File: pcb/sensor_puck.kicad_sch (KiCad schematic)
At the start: 35 parts, among them J1 Conn_01x07_Socket, J2 Conn_01x07_Socket, J3 USB_C_Receptacle_USB2.0_16P, SW1 RST, SW2 BOOT, U1 ESP32-S3-MINI-1U, U2 LIS3MDL, U3 LSM6DSOXTR, U4 STC31-C-R3

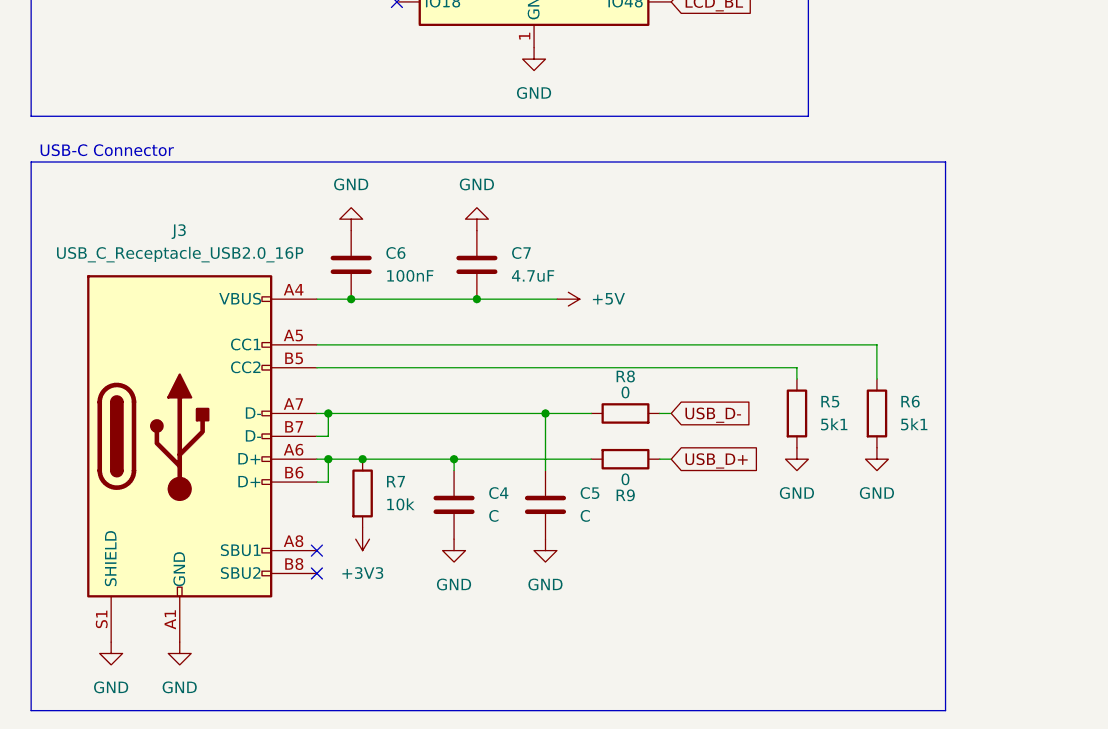
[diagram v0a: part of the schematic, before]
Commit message: fix(pcb): improve USB-C wiring and routing
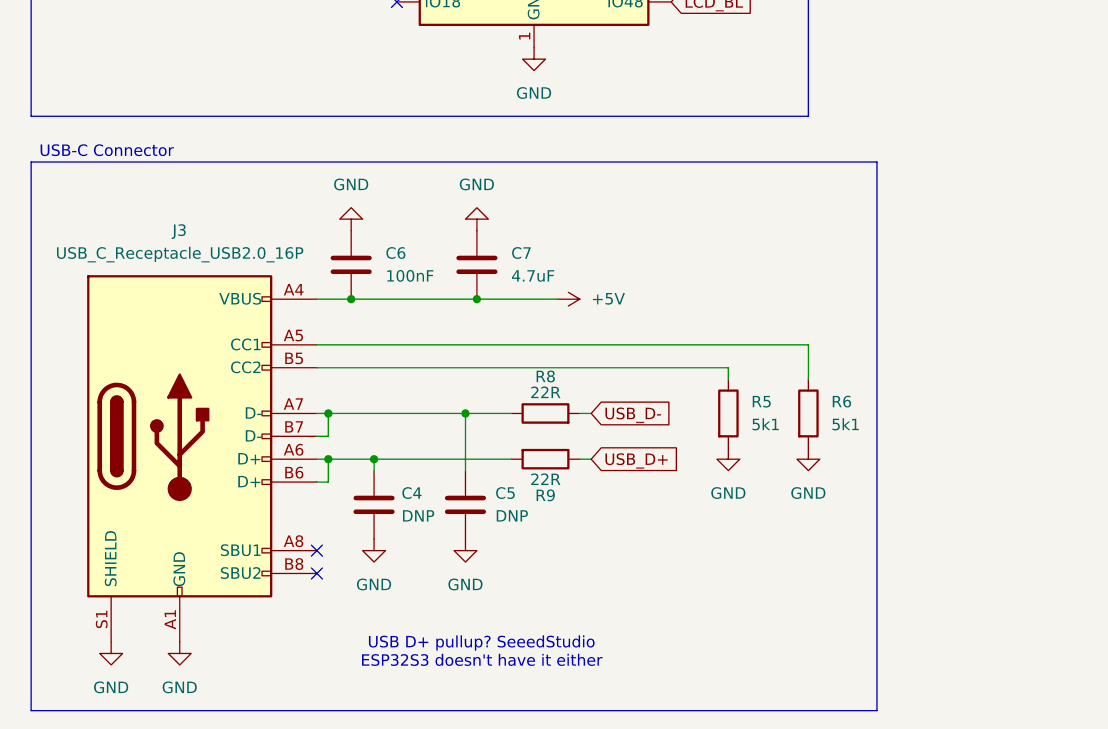
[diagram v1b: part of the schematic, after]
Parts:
- removed R7: 10k, Resistor_SMD:R_0805_2012Metric, symbol Device:R
- C4, C5: value C -> DNP
- R8, R9: value 0 -> 22R
- SW1, SW2: footprint Button_Switch_SMD:SW_Push_1P1T_NO_6x6mm_H9.5mm -> Button_Switch_THT:SW_PUSH_6mm
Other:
- note added: "USB D+ pullup? SeeedStudio ESP32S3 doesn't have it either"
- moved on the sheet: C4, C5, R5, R6, R8, R9

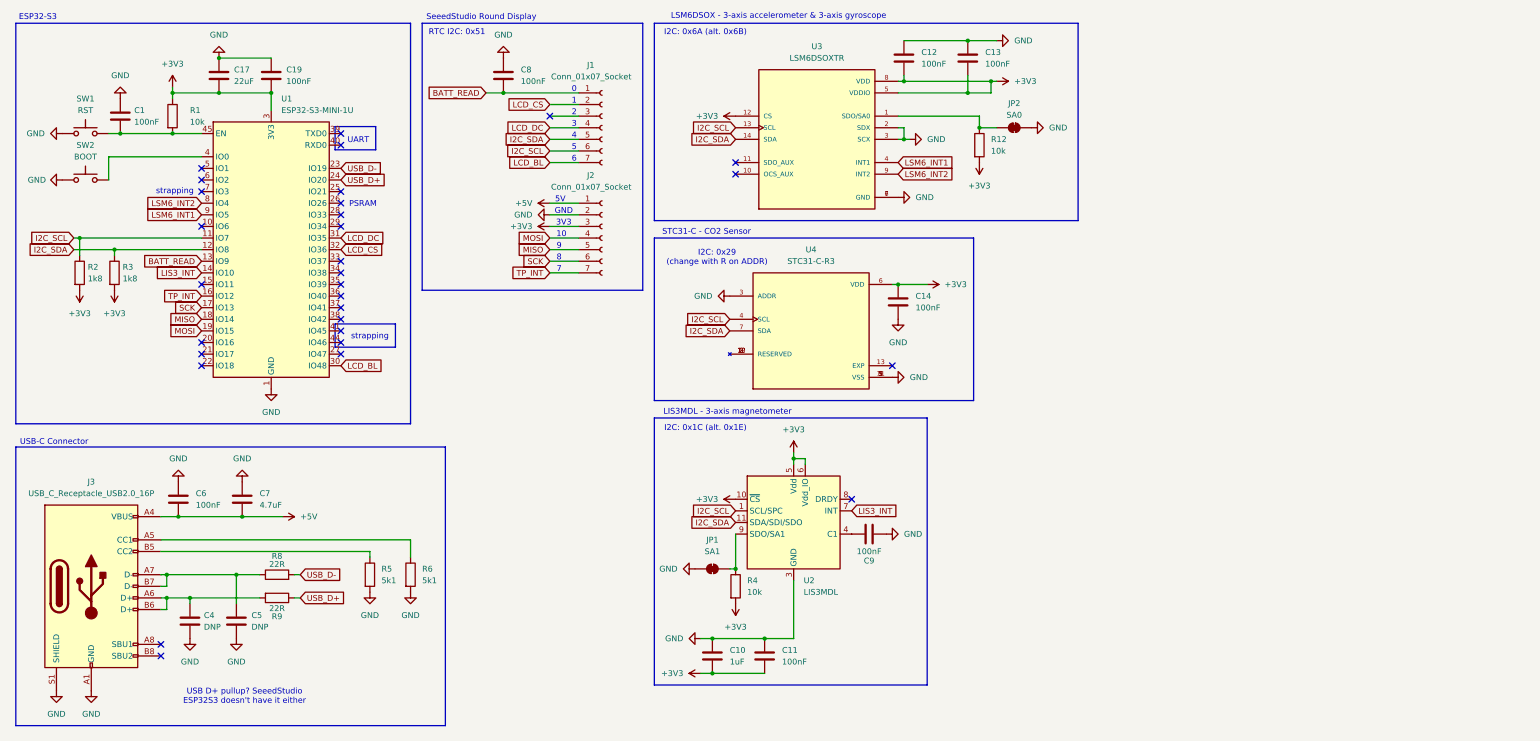
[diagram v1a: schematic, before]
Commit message: feat(pcb): VBUS -> 3V3 regulator, BME288, general improvements
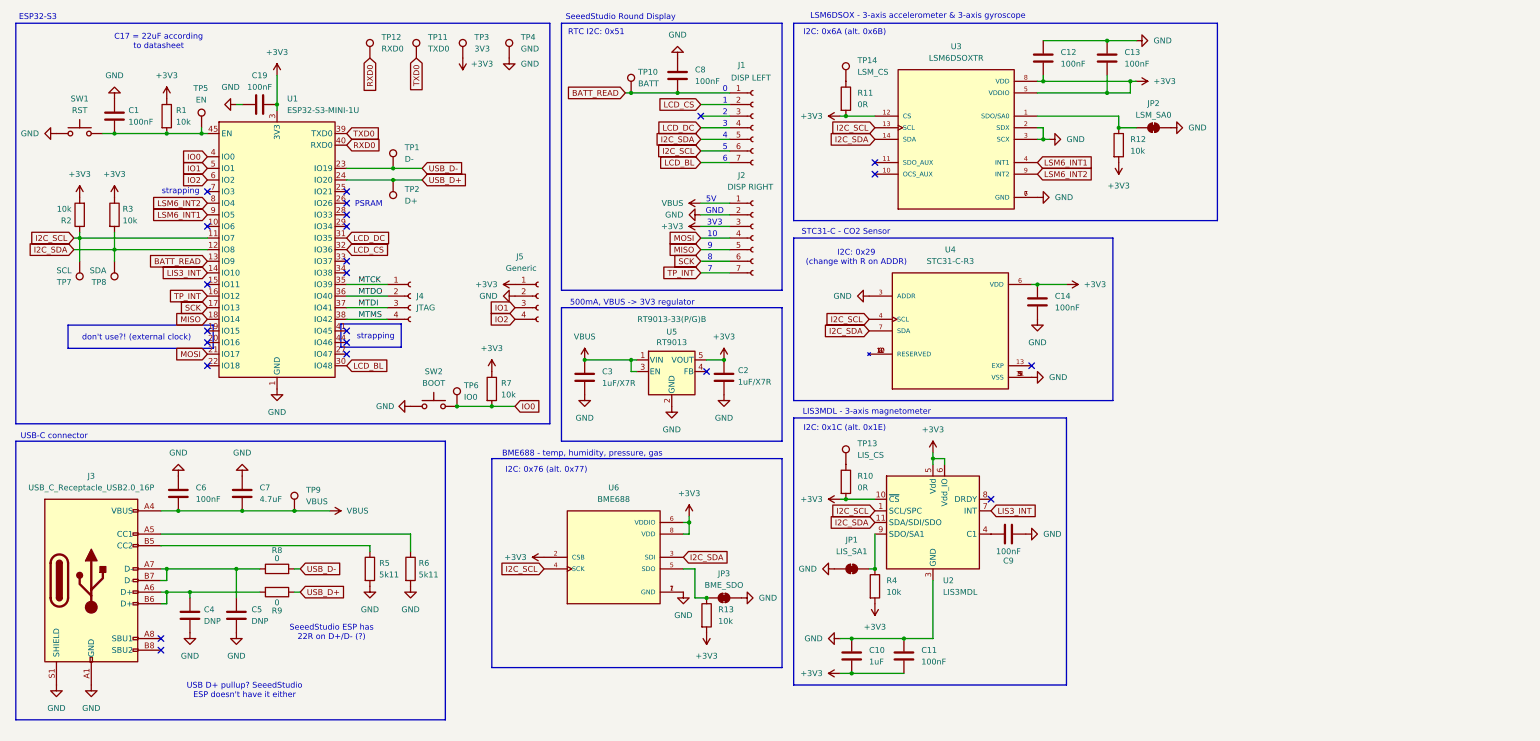
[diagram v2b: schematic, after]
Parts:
- removed C17: 22uF, Capacitor_SMD:C_0805_2012Metric, symbol Device:C
- added C2, C3: 1uF/X7R, Capacitor_SMD:C_0805_2012Metric, symbol Device:C
- added J4: JTAG, Connector_PinHeader_2.54mm:PinHeader_1x04_P2.54mm_Vertical, symbol Connector:Conn_01x04_Socket
- added J5: Generic, Connector_PinHeader_2.54mm:PinHeader_1x04_P2.54mm_Vertical, symbol Connector:Conn_01x04_Socket
- added JP3: BME_SDO, Jumper:SolderJumper-2_P1.3mm_Bridged_RoundedPad1.0x1.5mm, symbol Jumper:SolderJumper_2_Bridged
- added R10, R11: 0R, Resistor_SMD:R_0805_2012Metric, symbol Device:R
- added R13, R7: 10k, Resistor_SMD:R_0805_2012Metric, symbol Device:R
- added TP1: D-, TestPoint:TestPoint_Pad_D1.0mm, symbol Connector:TestPoint
- added TP10: BATT, TestPoint:TestPoint_Pad_D1.0mm, symbol Connector:TestPoint
- added TP11: TXD0, TestPoint:TestPoint_Pad_D1.0mm, symbol Connector:TestPoint
- added TP12: RXD0, TestPoint:TestPoint_Pad_D1.0mm, symbol Connector:TestPoint
- added TP13: LIS_CS, TestPoint:TestPoint_Pad_1.0x1.0mm, symbol Connector:TestPoint
- added TP14: LSM_CS, TestPoint:TestPoint_Pad_1.0x1.0mm, symbol Connector:TestPoint
- added TP2: D+, TestPoint:TestPoint_Pad_D1.0mm, symbol Connector:TestPoint
- added TP3: 3V3, TestPoint:TestPoint_Pad_D1.0mm, symbol Connector:TestPoint
- added TP4: GND, TestPoint:TestPoint_Pad_D1.0mm, symbol Connector:TestPoint
- added TP5: EN, TestPoint:TestPoint_Pad_D1.0mm, symbol Connector:TestPoint
- added TP6: IO0, TestPoint:TestPoint_Pad_D1.0mm, symbol Connector:TestPoint
- added TP7: SCL, TestPoint:TestPoint_Pad_D1.0mm, symbol Connector:TestPoint
- added TP8: SDA, TestPoint:TestPoint_Pad_D1.0mm, symbol Connector:TestPoint
- added TP9: VBUS, TestPoint:TestPoint_Pad_D1.0mm, symbol Connector:TestPoint
- added U5: RT9013, Package_TO_SOT_SMD:SOT-23-5, symbol Regulator_Linear:TPS72201
- added U6: BME688, BME688:IC_BME688, symbol BME688:BME688
- J1: value Conn_01x07_Socket -> DISP LEFT
- J2: value Conn_01x07_Socket -> DISP RIGHT
- JP1: value SA1 -> LIS_SA1; footprint Jumper:SolderJumper-2_P1.3mm_Bridged_Pad1.0x1.5mm -> Jumper:SolderJumper-2_P1.3mm_Bridged_RoundedPad1.0x1.5mm
- JP2: value SA0 -> LSM_SA0; footprint Jumper:SolderJumper-2_P1.3mm_Bridged_Pad1.0x1.5mm -> Jumper:SolderJumper-2_P1.3mm_Bridged_RoundedPad1.0x1.5mm
- R2, R3: value 1k8 -> 10k
- R5, R6: value 5k1 -> 5k11
- R8, R9: value 22R -> 0
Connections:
- net +3V3: now also R3.1, C2.2, J5.1 (Pin_1), R10.2, R11.2, R13.2, R7.1, TP3.1, U5.5 (VOUT), U6.2 (CSB), U6.6 (VDDIO), U6.8 (VDD); no longer R3.2
- net BATT_READ: now also TP10.1
- net GND: now also C2.1, C3.1, J5.2 (Pin_2), JP3.2 (B), TP4.1, U5.2 (GND), U6.1 (GND), U6.7 (GND)
- net I2C_SCL: now also TP7.1, U6.4 (SCK)
- net I2C_SDA: now also R3.2, TP8.1, U6.3 (SDI); no longer R3.1
- net MOSI: now also U1.21 (IO17); no longer U1.19 (IO15)
- net USB_D+: now also TP2.1
- net USB_D-: now also TP1.1
- net at C1.2, R1.2, SW1.2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: now also TP5.1
- net MTCK: now reaches U1.35 (IO39)
- net MTCK: now also J4.1 (Pin_1)
- net MTDO: now reaches U1.36 (IO40)
- net MTDO: now also J4.2 (Pin_2)
- net MTDI: now reaches U1.37 (IO41)
- net MTDI: now also J4.3 (Pin_3)
- net MTMS: now reaches U1.38 (IO42)
- net MTMS: now also J4.4 (Pin_4)
- net TXD0: now reaches U1.39 (TXD0)
- net TXD0: now also TP11.1
- net IO0: now reaches SW2.2, U1.4 (IO0)
- net IO0: now also R7.2, TP6.1
- net RXD0: now reaches U1.40 (RXD0)
- net RXD0: now also TP12.1
- net IO1: now reaches U1.5 (IO1)
- net IO1: now also J5.3 (Pin_3)
- net IO2: now reaches U1.6 (IO2)
- net IO2: now also J5.4 (Pin_4)
- net +5V renamed VBUS
- net VBUS: now also C3.2, TP9.1, U5.1 (VIN), U5.3 (EN)
- new net: JP3.1 (A), R13.1, U6.5 (SDO)
- new net: R10.1, TP13.1
- new net: R11.1, TP14.1
- no-connect marks 30 -> 23
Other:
- note added: "500mA, VBUS -> 3V3 regulator"
- note added: "BME688 - temp, humidity, pressure, gas"
- note added: "C17 = 22uF according to datasheet"
- note added: "I2C: 0x76 (alt. 0x77)"
- note added: "SeeedStudio ESP has 22R on D+/D- (?)"
- note added: "USB D+ pullup? SeeedStudio ESP doesn't have it either"
- note added: "USB-C connector"
- note added: "don't use?! (external clock)"
- note removed: "UART"
- note removed: "USB D+ pullup? SeeedStudio ESP32S3 doesn't have it either"
- note removed: "USB-C Connector"
- moved on the sheet: C1, C10, C11, C12, C13, C14, C4, C5, C6, C7, C8, C9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

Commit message: feat(pcb): route PCB
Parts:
- removed J4: JTAG, Connector_PinHeader_2.54mm:PinHeader_1x04_P2.54mm_Vertical, symbol Connector:Conn_01x04_Socket
- removed TP10: BATT, TestPoint:TestPoint_Pad_D1.0mm, symbol Connector:TestPoint
- added C15, C16: 100nF, Capacitor_SMD:C_0805_2012Metric, symbol Device:C
- added R14: 0R, Resistor_SMD:R_0805_2012Metric, symbol Device:R
- added TP15: BME_CSB, TestPoint:TestPoint_Pad_D1.0mm, symbol Connector:TestPoint
- added TP16: MTCK, TestPoint:TestPoint_Pad_D1.0mm, symbol Connector:TestPoint
- added TP17: MTDO, TestPoint:TestPoint_Pad_D1.0mm, symbol Connector:TestPoint
- added TP18: MTDI, TestPoint:TestPoint_Pad_D1.0mm, symbol Connector:TestPoint
- added TP19: MTMS, TestPoint:TestPoint_Pad_D1.0mm, symbol Connector:TestPoint
- TP13, TP14: footprint TestPoint:TestPoint_Pad_1.0x1.0mm -> TestPoint:TestPoint_Pad_D1.0mm
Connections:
- net +3V3: now also R10.1, R11.1, C15.2, C16.2, R14.2; no longer R10.2, R11.2, U2.10 (~{CS}), U3.12 (CS), U6.2 (CSB)
- net GND: now also U4.13 (EXP), C15.1, C16.1
- net at TP13.1: now also R10.2, U2.10 (~{CS}); no longer R10.1
- net at TP14.1: now also R11.2, U3.12 (CS); no longer R11.1
- net MTCK: no longer names the net of U1.35 (IO39)
- net MTCK: now also TP16.1
- net MTDI: no longer names the net of U1.37 (IO41)
- net MTDI: now also TP18.1
- net MTDO: no longer names the net of U1.36 (IO40)
- net MTDO: now also TP17.1
- net MTMS: no longer names the net of U1.38 (IO42)
- net MTMS: now also TP19.1
- new net: R14.1, TP15.1, U6.2 (CSB)
- no-connect marks 23 -> 20
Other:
- moved on the sheet: JP3, R10, R11, R13, TP13, TP14, U6

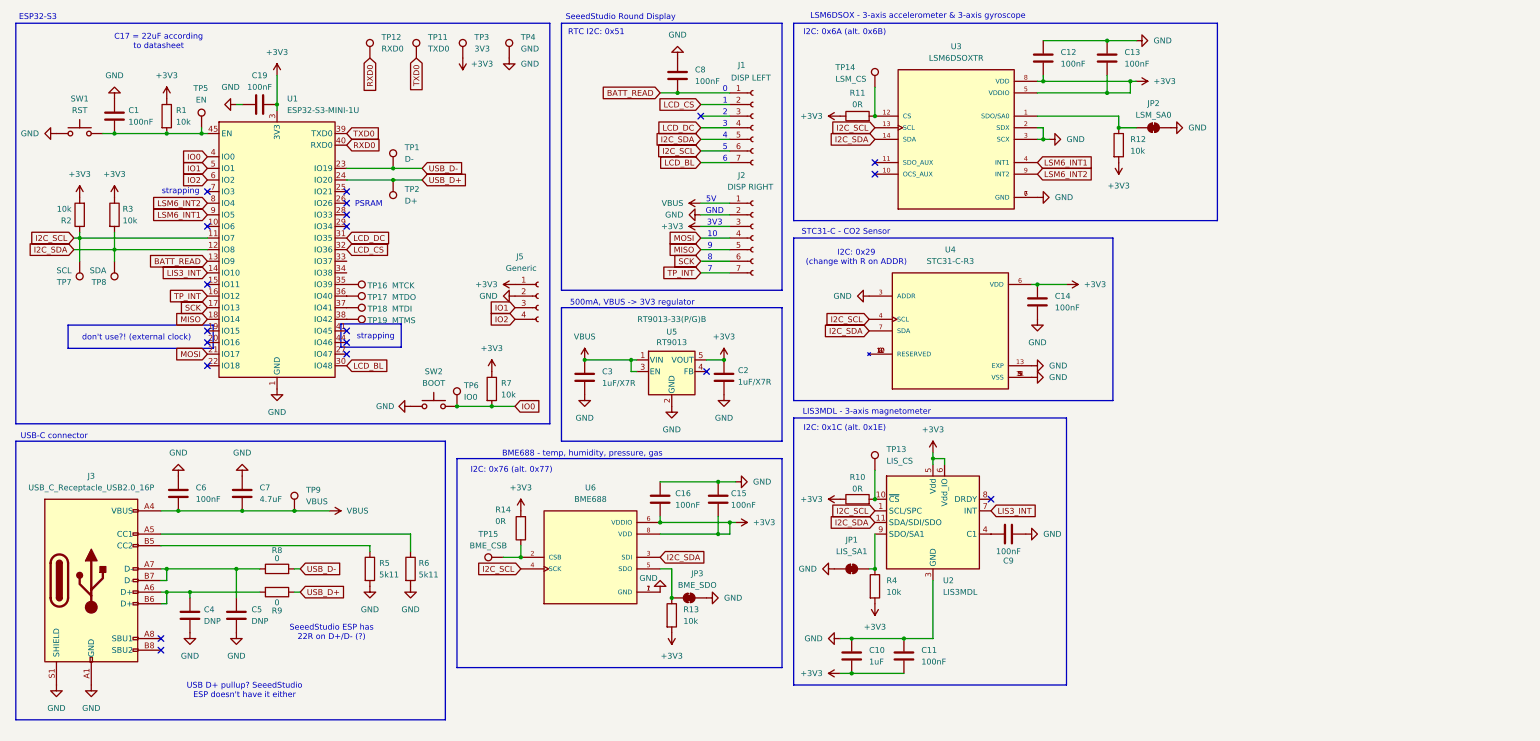
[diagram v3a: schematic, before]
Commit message: feat(pcb): make display's SD-Card slot usable
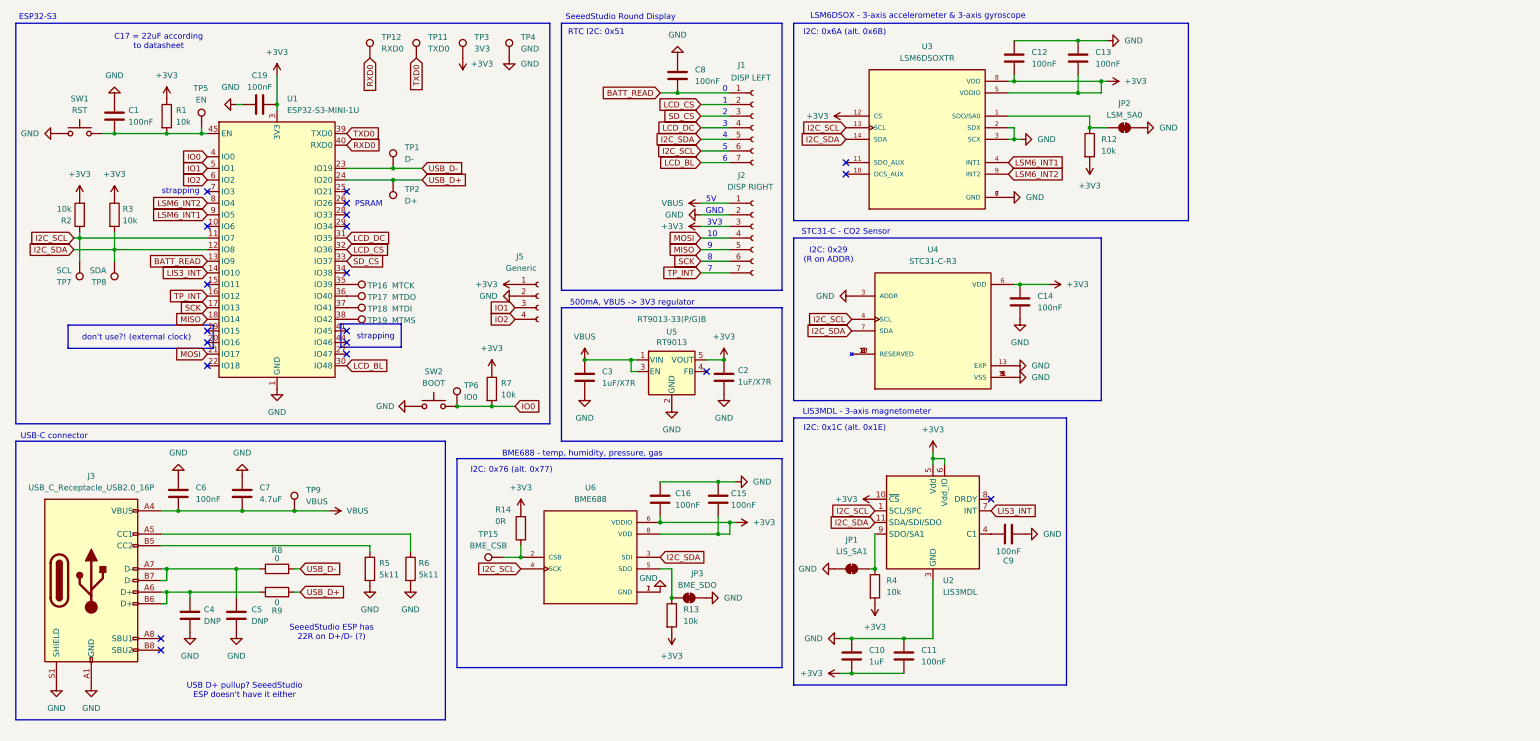
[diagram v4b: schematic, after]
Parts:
- removed R10, R11: 0R, Resistor_SMD:R_0805_2012Metric, symbol Device:R
- removed TP13: LIS_CS, TestPoint:TestPoint_Pad_D1.0mm, symbol Connector:TestPoint
- removed TP14: LSM_CS, TestPoint:TestPoint_Pad_D1.0mm, symbol Connector:TestPoint
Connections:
- net +3V3: now also U2.10 (~{CS}), U3.12 (CS)
- net SD_CS: now reaches J1.3 (Pin_3)
- net SD_CS: now also U1.33 (IO37)
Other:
- note added: "I2C: 0x29 (R on ADDR)"
- note removed: "I2C: 0x29 (change with R on ADDR)"
- moved on the sheet: C12, C13, C14, JP2, R12, U3, U4

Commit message: fix(pcb): add pulldown for LCD_BL pin
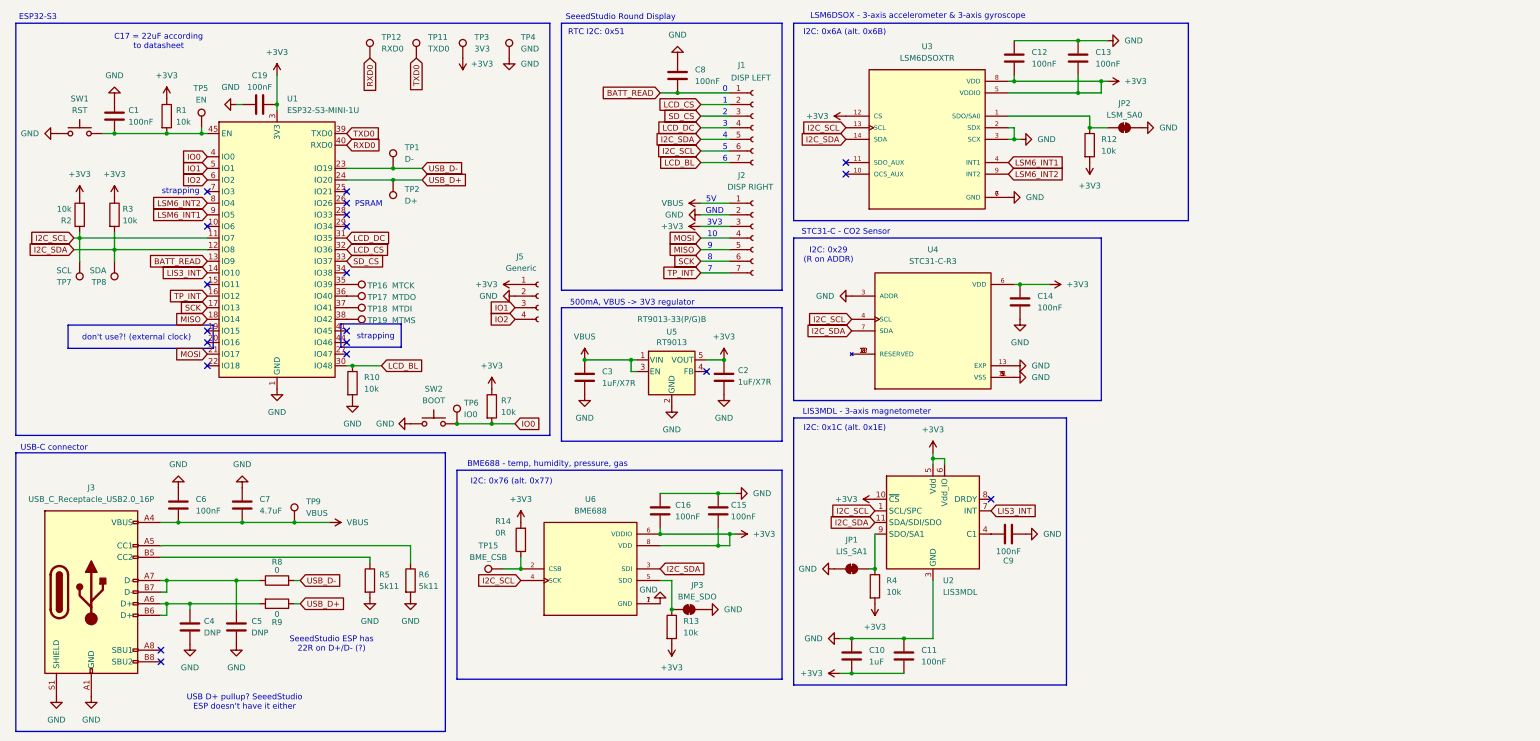
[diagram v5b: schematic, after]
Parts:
- added R10: 10k, symbol Device:R
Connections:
- net GND: now also R10.2
- net LCD_BL: now also R10.1
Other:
- moved on the sheet: C15, C16, C4, C5, C6, C7, J3, JP3, R13, R14, R5, R6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
